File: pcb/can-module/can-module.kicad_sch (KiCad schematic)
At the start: 27 parts, among them J10 MKDS-1,5-2-5.08, J11 MKDS-1,5-2-5.08, J12 MKDS-1,5-2-5.08, J13 MKDS-1,5-2-5.08, J14 MKDS-1,5-2-5.08, J4 MKDS-1,5-2-5.08, J6 MKDS-1,5-2-5.08, J7 MKDS-1,5-2-5.08, J8 MKDS-1,5-2-5.08, J9 MKDS-1,5-2-5.08, U1 AP2112K-3.3, U3 TPS2116DRL, U7 L78M05ABDT-TR

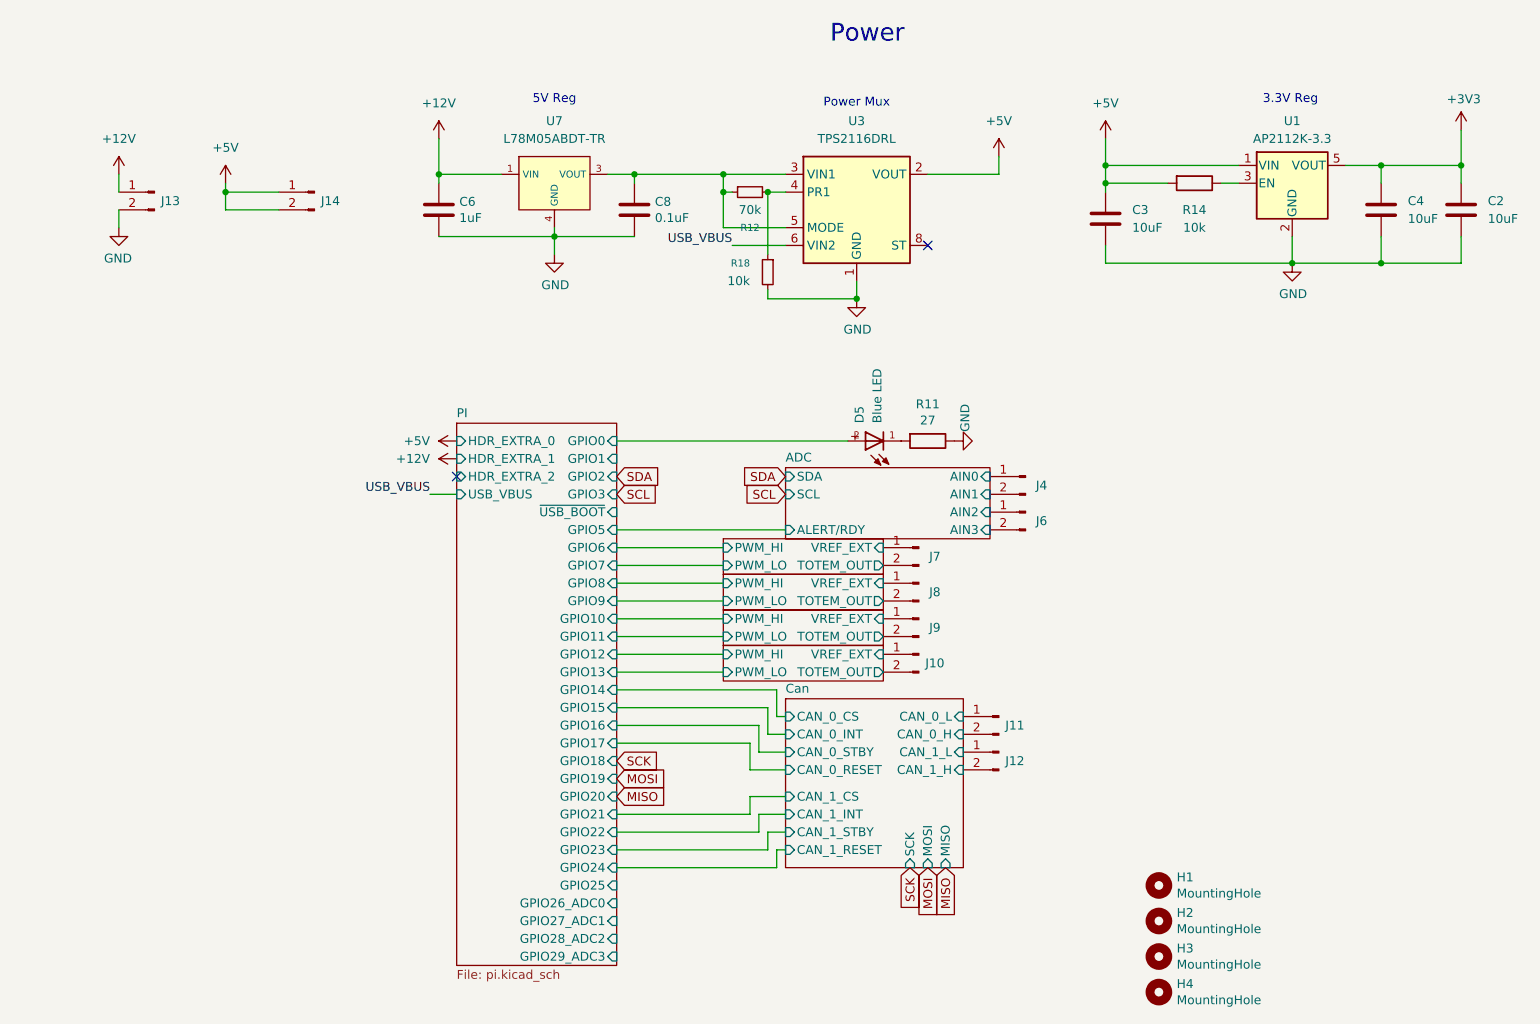
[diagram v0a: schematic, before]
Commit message: Fix ERC errors
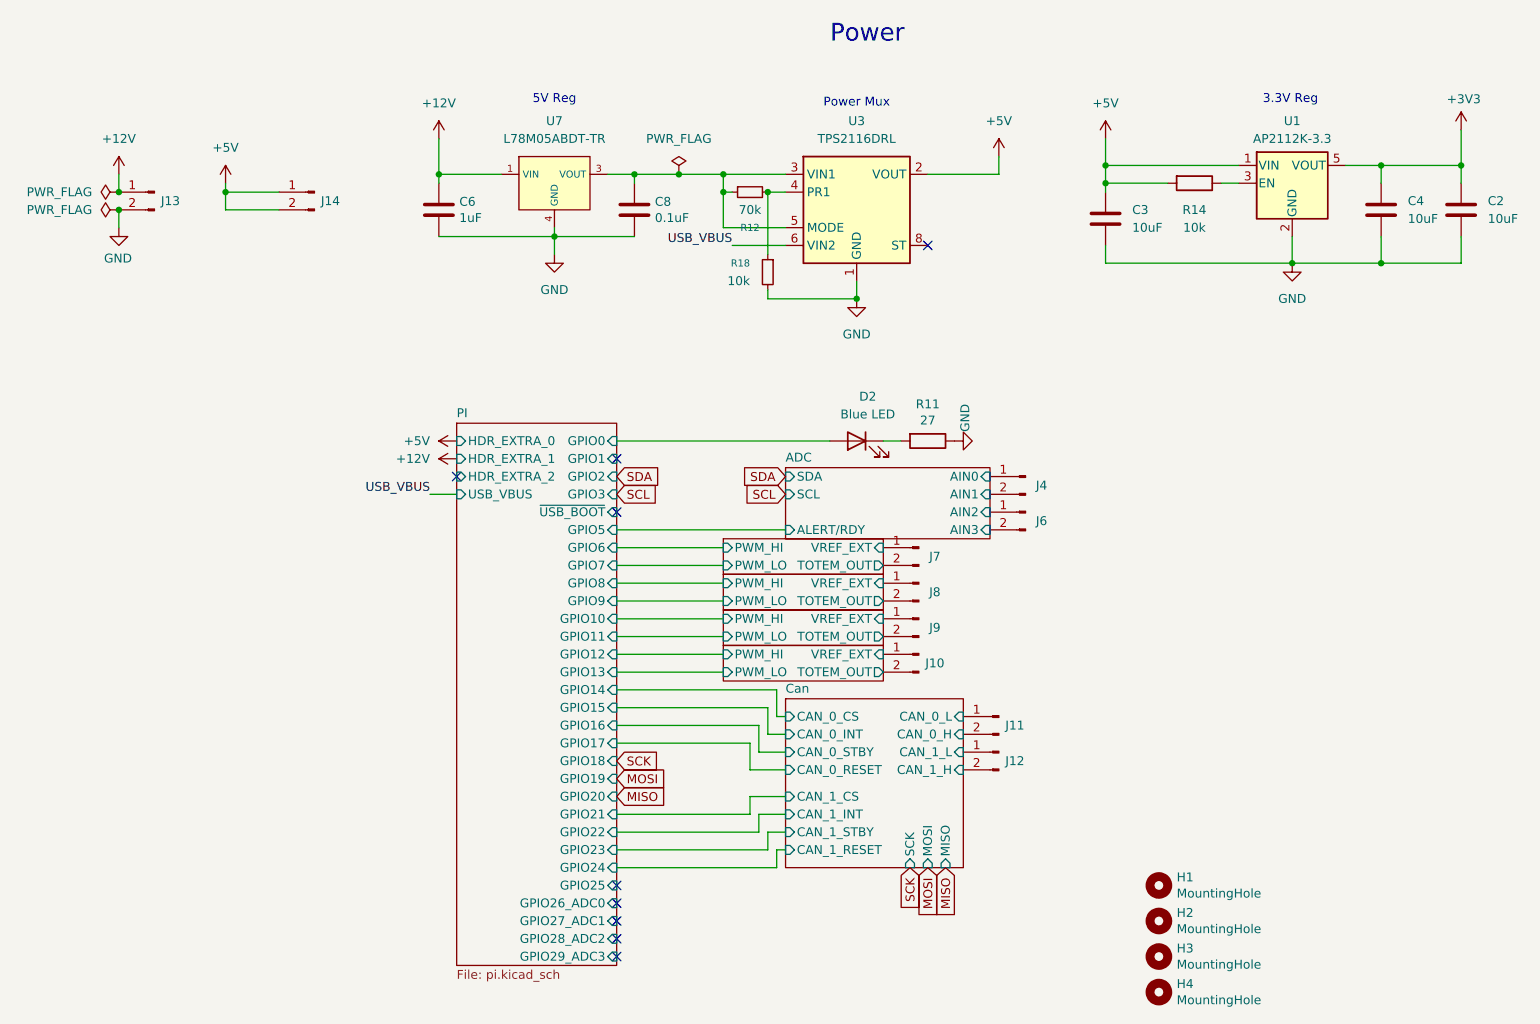
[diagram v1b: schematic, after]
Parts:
- removed D5: Blue LED, PCM_JLCPCB:D_0603, symbol Snapeda:WL-SMSW_0603_REC
- added D2: Blue LED, PCM_JLCPCB:D_0603, symbol Device:LED
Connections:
- net PI/GPIO0: now also D2.2 (A)
- net at R11.2: now also D2.1 (K)
- no-connect marks 2 -> 9

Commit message: Board layout
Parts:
- U4: renamed from U3; LCSC C82344 -> C3235557
- renumbered C8 to C1, C6 to C2, C3 to C25, C4 to C26, C2 to C27, H4 to H1, H1 to H3, H3 to H4, J12 to J1, J6 to J10, J4 to J11, J11 to J2, J13 to J3, J14 to J4, J10 to J5, J9 to J7, J7 to J9, R14 to R27, R11 to R30, R12 to R4, R18 to R5, U7 to U1, U1 to U7
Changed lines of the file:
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@@
 		(on_board yes)
 		(dnp no)
-		(property "Reference" "H1"
+		(property "Reference" "H3"
 			(at 262.89 151.2316 0)
 			(effects
@@
 			(project "can-module"
 				(path "/8c0b3d8b-46d3-4173-ab1e-a61765f77d61"
-					(reference "H1")
+					(reference "H3")
 					(unit 1)
 				)
@@
 		(on_board yes)
 		(dnp no)
-		(property "Reference" "H3"
+		(property "Reference" "H4"
 			(at 262.89 161.3916 0)
 			(effects
@@
 			(project "can-module"
 				(path "/8c0b3d8b-46d3-4173-ab1e-a61765f77d61"
-					(reference "H3")
+					(reference "H4")
 					(unit 1)
 				)
@@
 		(on_board yes)
 		(dnp no)
-		(property "Reference" "H4"
+		(property "Reference" "H1"
 			(at 262.89 166.4716 0)
 			(effects
@@
 			(project "can-module"
 				(path "/8c0b3d8b-46d3-4173-ab1e-a61765f77d61"
-					(reference "H4")
+					(reference "H1")
 					(unit 1)
 				)
@@
 		(on_board yes)
 		(dnp no)
-		(property "Reference" "J11"
+		(property "Reference" "J2"
 			(at 239.776 129.54 0)
 			(effects
@@
 			(project "can-module"
 				(path "/8c0b3d8b-46d3-4173-ab1e-a61765f77d61"
-					(reference "J11")
+					(reference "J2")
 					(unit 1)
 				)
@@
 		(on_board yes)
 		(dnp no)
-		(property "Reference" "R11"
+		(property "Reference" "R30"
 			(at 227.33 83.6422 90)
 			(effects
@@
 			(project "can-module"
 				(path "/8c0b3d8b-46d3-4173-ab1e-a61765f77d61"
-					(reference "R11")
+					(reference "R30")
 					(unit 1)
 				)
@@
 		(dnp no)
 		(fields_autoplaced yes)
-		(property "Reference" "U7"
+		(property "Reference" "U1"
 			(at 173.99 43.18 0)
 			(effects
@@
 			(project "can-module"
 				(path "/8c0b3d8b-46d3-4173-ab1e-a61765f77d61"
-					(reference "U7")
+					(reference "U1")
 					(unit 1)
 				)
@@
 		(on_board yes)
 		(dnp no)
-		(property "Reference" "J6"
+		(property "Reference" "J10"
 			(at 243.586 100.33 0)
 			(effects
@@
 			(project "can-module"
 				(path "/8c0b3d8b-46d3-4173-ab1e-a61765f77d61"
-					(reference "J6")
+					(reference "J10")
 					(unit 1)
 				)
@@
 		(on_board yes)
 		(dnp no)
-		(property "Reference" "R12"
+		(property "Reference" "R4"
 			(at 201.93 58.42 90)
 			(effects
@@
 			(project "can-module"
 				(path "/8c0b3d8b-46d3-4173-ab1e-a61765f77d61"
-					(reference "R12")
+					(reference "R4")
 					(unit 1)
 				)
@@
 		(dnp no)
 		(fields_autoplaced yes)
-		(property "Reference" "U1"
+		(property "Reference" "U7"
 			(at 279.4 43.18 0)
 			(effects
@@
 			(project "can-module"
 				(path "/8c0b3d8b-46d3-4173-ab1e-a61765f77d61"
-					(reference "U1")
+					(reference "U7")
 					(unit 1)
 				)
@@
 		(on_board yes)
 		(dnp no)
-		(property "Reference" "C3"
+		(property "Reference" "C25"
 			(at 256.54 55.8799 0)
 			(effects
@@
 			(project "can-module"
 				(path "/8c0b3d8b-46d3-4173-ab1e-a61765f77d61"
-					(reference "C3")
+					(reference "C25")
 					(unit 1)
 				)
@@
 		(on_board yes)
 		(dnp no)
-		(property "Reference" "J13"
+		(property "Reference" "J3"
 			(at 119.126 54.61 0)
 			(effects
@@
 			(project "can-module"
 				(path "/8c0b3d8b-46d3-4173-ab1e-a61765f77d61"
-					(reference "J13")
+					(reference "J3")
 					(unit 1)
 				)
@@
 		(on_board yes)
 		(dnp no)
-		(property "Reference" "J10"
+		(property "Reference" "J5"
 			(at 228.346 120.65 0)
 			(effects
@@
 			(project "can-module"
 				(path "/8c0b3d8b-46d3-4173-ab1e-a61765f77d61"
-					(reference "J10")
+					(reference "J5")
 					(unit 1)
 				)
@@
 		(on_board yes)
 		(dnp no)
-		(property "Reference" "J12"
+		(property "Reference" "J1"
 			(at 239.776 134.62 0)
 			(effects
@@
 			(project "can-module"
 				(path "/8c0b3d8b-46d3-4173-ab1e-a61765f77d61"
-					(reference "J12")
+					(reference "J1")
 					(unit 1)
 				)
@@
 		(on_board yes)
 		(dnp no)
-		(property "Reference" "R18"
+		(property "Reference" "R5"
 			(at 201.93 63.4999 0)
 			(effects
@@
 			(project "can-module"
 				(path "/8c0b3d8b-46d3-4173-ab1e-a61765f77d61"
-					(reference "R18")
+					(reference "R5")
 					(unit 1)
 				)
@@
 		(on_board yes)
 		(dnp no)
-		(property "Reference" "J4"
+		(property "Reference" "J11"
 			(at 243.586 95.25 0)
 			(effects
@@
 			(project "can-module"
 				(path "/8c0b3d8b-46d3-4173-ab1e-a61765f77d61"
-					(reference "J4")
+					(reference "J11")
 					(unit 1)
 				)
@@
 		(on_board yes)
 		(dnp no)
-		(property "Reference" "J14"
+		(property "Reference" "J4"
 			(at 141.986 54.61 0)
 			(effects
@@
 			(project "can-module"
 				(path "/8c0b3d8b-46d3-4173-ab1e-a61765f77d61"
-					(reference "J14")
+					(reference "J4")
 					(unit 1)
 				)
@@
 		(dnp no)
 		(fields_autoplaced yes)
-		(property "Reference" "R14"
+		(property "Reference" "R27"
 			(at 265.43 55.88 90)
 			(effects
@@
 			(project "can-module"
 				(path "/8c0b3d8b-46d3-4173-ab1e-a61765f77d61"
-					(reference "R14")
+					(reference "R27")
 					(unit 1)
 				)
@@
 		(on_board yes)
 		(dnp no)
-		(property "Reference" "J7"
+		(property "Reference" "J9"
 			(at 228.346 105.41 0)
 			(effects
@@
 			(project "can-module"
 				(path "/8c0b3d8b-46d3-4173-ab1e-a61765f77d61"
-					(reference "J7")
+					(reference "J9")
 					(unit 1)
 				)
@@
 		(dnp no)
 		(fields_autoplaced yes)
-		(property "Reference" "C2"
+		(property "Reference" "C27"
 			(at 307.34 54.6099 0)
 			(effects
@@
 			(project "can-module"
 				(path "/8c0b3d8b-46d3-4173-ab1e-a61765f77d61"
-					(reference "C2")
+					(reference "C27")
 					(unit 1)
 				)
@@
 		(on_board yes)
 		(dnp no)
-		(property "Reference" "C6"
+		(property "Reference" "C2"
 			(at 160.401 54.7116 0)
 			(effects
@@
 			(project "can-module"
 				(path "/8c0b3d8b-46d3-4173-ab1e-a61765f77d61"
-					(reference "C6")
+					(reference "C2")
 					(unit 1)
 				)
@@
 		(dnp no)
 		(fields_autoplaced yes)
-		(property "Reference" "U3"
+		(property "Reference" "U4"
 			(at 217.17 43.18 0)
 			(effects
@@
 			)
 		)
-		(property "LCSC" "C82344"
+		(property "LCSC" "C3235557"
 			(at 217.17 43.18 0)
 			(effects
@@
 			(project "can-module"
 				(path "/8c0b3d8b-46d3-4173-ab1e-a61765f77d61"
-					(reference "U3")
+					(reference "U4")
 					(unit 1)
 				)
@@
 		(on_board yes)
 		(dnp no)
-		(property "Reference" "J9"
+		(property "Reference" "J7"
 			(at 228.346 115.57 0)
 			(effects
@@
 			(project "can-module"
 				(path "/8c0b3d8b-46d3-4173-ab1e-a61765f77d61"
-					(reference "J9")
+					(reference "J7")
 					(unit 1)
 				)
@@
 		(on_board yes)
 		(dnp no)
-		(property "Reference" "C8"
+		(property "Reference" "C1"
 			(at 188.341 54.7116 0)
 			(effects
@@
 			(project "can-module"
 				(path "/8c0b3d8b-46d3-4173-ab1e-a61765f77d61"
-					(reference "C8")
+					(reference "C1")
 					(unit 1)
 				)
@@
 		(dnp no)
 		(fields_autoplaced yes)
-		(property "Reference" "C4"
+		(property "Reference" "C26"
 			(at 295.91 54.6099 0)
 			(effects
@@
 			(project "can-module"
 				(path "/8c0b3d8b-46d3-4173-ab1e-a61765f77d61"
-					(reference "C4")
+					(reference "C26")
 					(unit 1)
 				)

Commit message: E30 code
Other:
- note added: "FIX: THIS RESISTOR IS TOO LOW! PR1 needs to be at least 1V for switchover"
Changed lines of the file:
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@@
+		)
+	)
+	(text "FIX: THIS RESISTOR IS TOO LOW! PR1 needs to be at least 1V for switchover"
+		(exclude_from_sim no)
+		(at 219.202 68.58 0)
+		(effects
+			(font
+				(size 1.27 1.27)
+			)
 		)
 	)
